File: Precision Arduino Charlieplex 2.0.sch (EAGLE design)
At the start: 265 parts, among them J402 EM406, J404 EM406, U401 ATMEGA328, U501 FT232RLSSOP, U602 ZF7, Y401 12.00

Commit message: Merged Mio's KwanSystems.lbr, updated all eagle files to use it.
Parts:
- removed D200, D201, D202, D203, D204, D205, D206, D207, D208, D209, D210, D211, D212, D213, D214, D215, D216, D217, D218, D219, D220, D221, D222, D223, D224, D225, D226, D227, D228, D229, D230, D231, D232, D233, D234, D235, D236, D237, D238, D239, D240, D241, D242, D243, D244, D245, D246, D247, D248, D249, D250, D251, D252, D253, D254, D255, D256, D257, D258, D259, D300, D301, D302, D303, D304, D305, D306, D307, D308, D309, D310, D311, D312, D313, D314, D315, D316, D317, D318, D319, D320, D321, D322, D323, D324, D325, D326, D327, D328, D329, D330, D331, D332, D333, D334, D335, D336, D337, D338, D339, D340, D341, D342, D343, D344, D345, D346, D347, D348, D349, D350, D351, D352, D353, D354, D355, D356, D357, D358, D359: HOUR, SparkFun:LED0603
- removed J402, J404: EM406, SparkFun:EM406
- removed SJ1: (no value), SparkFun:SOLDERJUMPER_2WAYS
- added D060, D061, D062: HOUR, SparkFun:LED0603
- added J001, J004: (no value), SparkFun:M04PTH
- added J005: (no value), SparkFun:M06SIP
- added J405, J406: (no value), SparkFun:M081X08
- added JP1, JP2, JP3, JP4: STAND-OFF, SparkFun:STAND-OFF
- added JP5: (no value), SparkFun:M02PTH
- D501: value RED -> BLUE
- D502: value BLUE -> RED
- S429: value B3U-1100P -> B3U-1000P; device KwanSystems:B3U-1100P -> KwanSystems:B3U-1000P
- Y401: value 12.00 -> 16MHz
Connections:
- new net 3V3: J004.4, JP5.1, U501.3V3OUT
- net AT_RX: no longer SJ1.2
- net AT_TX: now also J004.1; no longer J402.RX, J404.RX
- net D12: now also J005.5
- net GND: now also J001.4, J004.3, J005.3, S429.1; no longer J402.GND1, J402.GND2, J404.GND1, J404.GND2, S429G.1, S429S.1, Y401G$1.1
- net GPS_TX: now also J004.2; no longer J402.TX, J404.TX, SJ1.1
- net P01: now also J005.6
- net P16: now also J005.4
- net PPS: now also JP5.2; no longer J402.1PPS, J404.1PPS
- net Q01: now also D060.A, D061.A, J406.1; no longer D200.A, D215.A, D229.A, D242.A, D254.A, D305.A, D315.A, D324.A, D332.A, D339.A, D345.A, D350.A, D354.A, D357.A, D359.A
- net Q02: now also D062.A, J406.2; no longer D200.C, D201.A, D216.A, D230.A, D243.A, D255.A, D306.A, D316.A, D325.A, D333.A, D340.A, D346.A, D351.A, D355.A, D358.A
- net Q03: now also J406.3; no longer D201.C, D202.A, D215.C, D217.A, D231.A, D244.A, D256.A, D307.A, D317.A, D326.A, D334.A, D341.A, D347.A, D352.A, D356.A
- net Q04: now also J406.4; no longer D202.C, D203.A, D216.C, D218.A, D229.C, D232.A, D245.A, D257.A, D308.A, D318.A, D327.A, D335.A, D342.A, D348.A, D353.A
- net Q05: now also J406.5; no longer D203.C, D204.A, D217.C, D219.A, D230.C, D233.A, D242.C, D246.A, D258.A, D309.A, D319.A, D328.A, D336.A, D343.A, D349.A
- net Q06: now also J406.6; no longer D204.C, D205.A, D218.C, D220.A, D231.C, D234.A, D243.C, D247.A, D254.C, D259.A, D310.A, D320.A, D329.A, D337.A, D344.A
- net Q07: now also J406.7; no longer D205.C, D206.A, D219.C, D221.A, D232.C, D235.A, D244.C, D248.A, D255.C, D300.A, D305.C, D311.A, D321.A, D330.A, D338.A
- net Q08: now also J406.8; no longer D206.C, D207.A, D220.C, D222.A, D233.C, D236.A, D245.C, D249.A, D256.C, D301.A, D306.C, D312.A, D315.C, D322.A, D331.A
- net Q09: now also J405.1; no longer D207.C, D208.A, D221.C, D223.A, D234.C, D237.A, D246.C, D250.A, D257.C, D302.A, D307.C, D313.A, D316.C, D323.A, D324.C
- net Q10: now also J405.2; no longer D208.C, D209.A, D222.C, D224.A, D235.C, D238.A, D247.C, D251.A, D258.C, D303.A, D308.C, D314.A, D317.C, D325.C, D332.C
- net Q11: now also J405.3; no longer D209.C, D210.A, D223.C, D225.A, D236.C, D239.A, D248.C, D252.A, D259.C, D304.A, D309.C, D318.C, D326.C, D333.C, D339.C
- net Q12: now also J405.4; no longer D210.C, D211.A, D224.C, D226.A, D237.C, D240.A, D249.C, D253.A, D300.C, D310.C, D319.C, D327.C, D334.C, D340.C, D345.C
- net Q13: now also J405.5; no longer D211.C, D212.A, D225.C, D227.A, D238.C, D241.A, D250.C, D301.C, D311.C, D320.C, D328.C, D335.C, D341.C, D346.C, D350.C
- net Q14: now also J405.6; no longer D212.C, D213.A, D226.C, D228.A, D239.C, D251.C, D302.C, D312.C, D321.C, D329.C, D336.C, D342.C, D347.C, D351.C, D354.C
- net Q15: now also J405.7; no longer D213.C, D214.A, D227.C, D240.C, D252.C, D303.C, D313.C, D322.C, D330.C, D337.C, D343.C, D348.C, D352.C, D355.C, D357.C
- net Q16: now also J405.8; no longer D214.C, D228.C, D241.C, D253.C, D304.C, D314.C, D323.C, D331.C, D338.C, D344.C, D349.C, D353.C, D356.C, D358.C, D359.C
- net RESET: now also J005.1, S429.2; no longer S429S.2
- net USBD+: now also J001.1
- net USBD-: now also J001.2
- net USB_TX: no longer SJ1.3
- net VCC: now also J001.3, J005.2; no longer J402.VCC, J404.VCC
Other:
- moved on the sheet: C010, C408, D000, D001, D002, D003, D004, D005, D006, D007, D008, D009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

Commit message: Preparing for check against workspace~ and workspace2
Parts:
- removed D060, D061, D062: HOUR, SparkFun:LED0603
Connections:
- net GND: now also Y401.GND
- net Q01: no longer D060.A, D061.A
- net Q02: no longer D062.A
- net XTAL1: now also Y401.1; no longer Y401_.1
- net XTAL2: now also Y401.2; no longer Y401_.2
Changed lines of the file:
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@@
 <part name="JP5" library="SparkFun" deviceset="M02" device="PTH"/>
 <part name="GND3" library="SparkFun" deviceset="GND" device=""/>
-<part name="D060" library="SparkFun" deviceset="LED" device="0603" value="HOUR"/>
-<part name="D061" library="SparkFun" deviceset="LED" device="0603" value="HOUR"/>
-<part name="D062" library="SparkFun" deviceset="LED" device="0603" value="HOUR"/>
 </parts>
 <sheets>
@@
 <instance part="C408" gate="G$1" x="-254" y="88.9" rot="R90"/>
 <instance part="GND4" gate="1" x="-261.62" y="53.34"/>
-<instance part="Y401" gate="_" x="-246.38" y="91.44" rot="R270"/>
+<instance part="Y401" gate="G$1" x="-246.38" y="91.44" rot="R270"/>
 <instance part="J001" gate="G$1" x="-149.86" y="147.32" rot="MR180"/>
 <instance part="J002" gate="G$1" x="-137.16" y="147.32" rot="MR180"/>
@@
 <instance part="JP5" gate="G$1" x="-129.54" y="50.8" rot="R180"/>
 <instance part="GND3" gate="1" x="-154.94" y="55.88" rot="MR0"/>
-<instance part="D060" gate="G$1" x="142.24" y="25.4" smashed="yes" rot="R180">
-<attribute name="NAME" x="142.7226" y="22.86" size="1.778" layer="95" rot="R270"/>
-</instance>
-<instance part="D061" gate="G$1" x="132.08" y="25.4" smashed="yes" rot="R180">
-<attribute name="NAME" x="132.5626" y="22.86" size="1.778" layer="95" rot="R270"/>
-</instance>
-<instance part="D062" gate="G$1" x="132.08" y="38.1" smashed="yes" rot="R180">
-<attribute name="NAME" x="132.5626" y="35.56" size="1.778" layer="95" rot="R270"/>
-</instance>
 </instances>
 <busses>
@@
 <segment>
 <wire x1="-17.78" y1="22.86" x2="132.08" y2="22.86" width="0.1524" layer="91"/>
-<wire x1="132.08" y1="22.86" x2="139.7" y2="22.86" width="0.1524" layer="91"/>
 <wire x1="139.7" y1="22.86" x2="132.08" y2="22.86" width="0.1524" layer="91"/>
 <wire x1="132.08" y1="22.86" x2="129.54" y2="22.86" width="0.1524" layer="91"/>
@@
 <pinref part="D159" gate="G$1" pin="C"/>
 <pinref part="J406" gate="G$1" pin="1"/>
-<wire x1="139.7" y1="22.86" x2="142.24" y2="22.86" width="0.1524" layer="91"/>
-<wire x1="142.24" y1="22.86" x2="144.78" y2="22.86" width="0.1524" layer="91"/>
+<wire x1="139.7" y1="22.86" x2="144.78" y2="22.86" width="0.1524" layer="91"/>
 <wire x1="144.78" y1="22.86" x2="144.78" y2="-17.78" width="0.1524" layer="91"/>
 <wire x1="144.78" y1="-17.78" x2="30.48" y2="-17.78" width="0.1524" layer="91"/>
 <wire x1="30.48" y1="-17.78" x2="30.48" y2="-20.32" width="0.1524" layer="91"/>
 <label x="144.78" y="17.78" size="1.778" layer="95" rot="R90"/>
-<pinref part="D060" gate="G$1" pin="A"/>
-<junction x="142.24" y="22.86"/>
-<pinref part="D061" gate="G$1" pin="A"/>
 <junction x="132.08" y="22.86"/>
 </segment>
@@
 <pinref part="D000" gate="G$1" pin="A"/>
 <pinref part="J406" gate="G$1" pin="2"/>
-<wire x1="129.54" y1="35.56" x2="132.08" y2="35.56" width="0.1524" layer="91"/>
-<wire x1="132.08" y1="35.56" x2="134.62" y2="35.56" width="0.1524" layer="91"/>
+<wire x1="129.54" y1="35.56" x2="134.62" y2="35.56" width="0.1524" layer="91"/>
 <wire x1="134.62" y1="35.56" x2="134.62" y2="30.48" width="0.1524" layer="91"/>
 <wire x1="139.7" y1="30.48" x2="134.62" y2="30.48" width="0.1524" layer="91"/>
@@
 <label x="134.62" y="17.78" size="1.778" layer="95" rot="R90"/>
 <junction x="134.62" y="30.48"/>
-<pinref part="D062" gate="G$1" pin="A"/>
-<junction x="132.08" y="35.56"/>
 </segment>
 </net>
@@
 <wire x1="-259.08" y1="88.9" x2="-261.62" y2="88.9" width="0.1524" layer="91"/>
 <wire x1="-261.62" y1="88.9" x2="-261.62" y2="68.58" width="0.1524" layer="91"/>
-<wire x1="-261.62" y1="93.98" x2="-261.62" y2="88.9" width="0.1524" layer="91"/>
+<wire x1="-261.62" y1="93.98" x2="-261.62" y2="91.44" width="0.1524" layer="91"/>
+<wire x1="-261.62" y1="91.44" x2="-261.62" y2="88.9" width="0.1524" layer="91"/>
 <wire x1="-259.08" y1="93.98" x2="-261.62" y2="93.98" width="0.1524" layer="91"/>
 <wire x1="-261.62" y1="104.14" x2="-261.62" y2="93.98" width="0.1524" layer="91"/>
@@
 <pinref part="C420" gate="G$1" pin="2"/>
 <pinref part="S429" gate="G$1" pin="1"/>
+<pinref part="Y401" gate="G$1" pin="GND"/>
+<wire x1="-251.46" y1="91.44" x2="-261.62" y2="91.44" width="0.1524" layer="91"/>
+<junction x="-261.62" y="91.44"/>
 </segment>
 <segment>
@@
 <label x="-241.3" y="93.98" size="1.778" layer="95"/>
 <pinref part="C407" gate="G$1" pin="2"/>
-<pinref part="Y401" gate="_" pin="1"/>
+<pinref part="Y401" gate="G$1" pin="1"/>
 <pinref part="U401" gate="G$1" pin="PB6(XTAL1/TOSC1)"/>
 </segment>
@@
 <label x="-241.3" y="78.74" size="1.778" layer="95"/>
 <pinref part="C408" gate="G$1" pin="2"/>
-<pinref part="Y401" gate="_" pin="2"/>
+<pinref part="Y401" gate="G$1" pin="2"/>
 <pinref part="U401" gate="G$1" pin="PB7(XTAL2/TOSC2)"/>
 </segment>

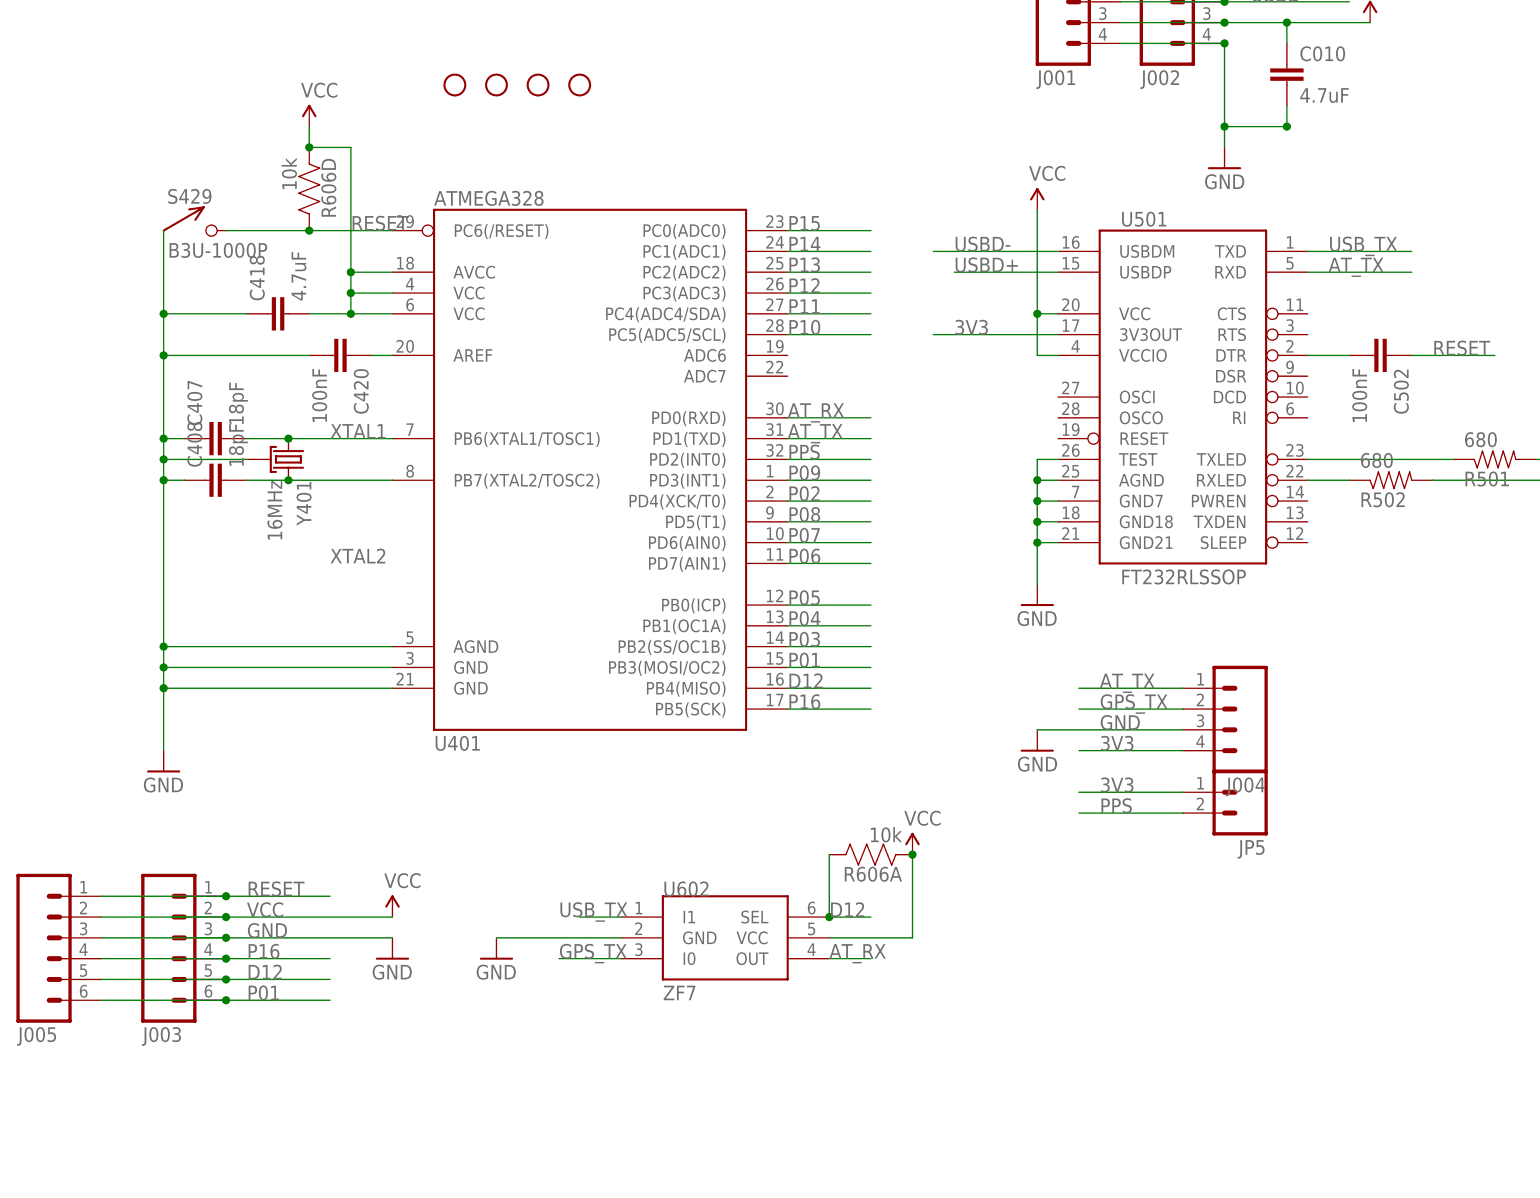
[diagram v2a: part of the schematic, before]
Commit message: Started RocketometerATMega.sch, finished PrecisionATMega32U4
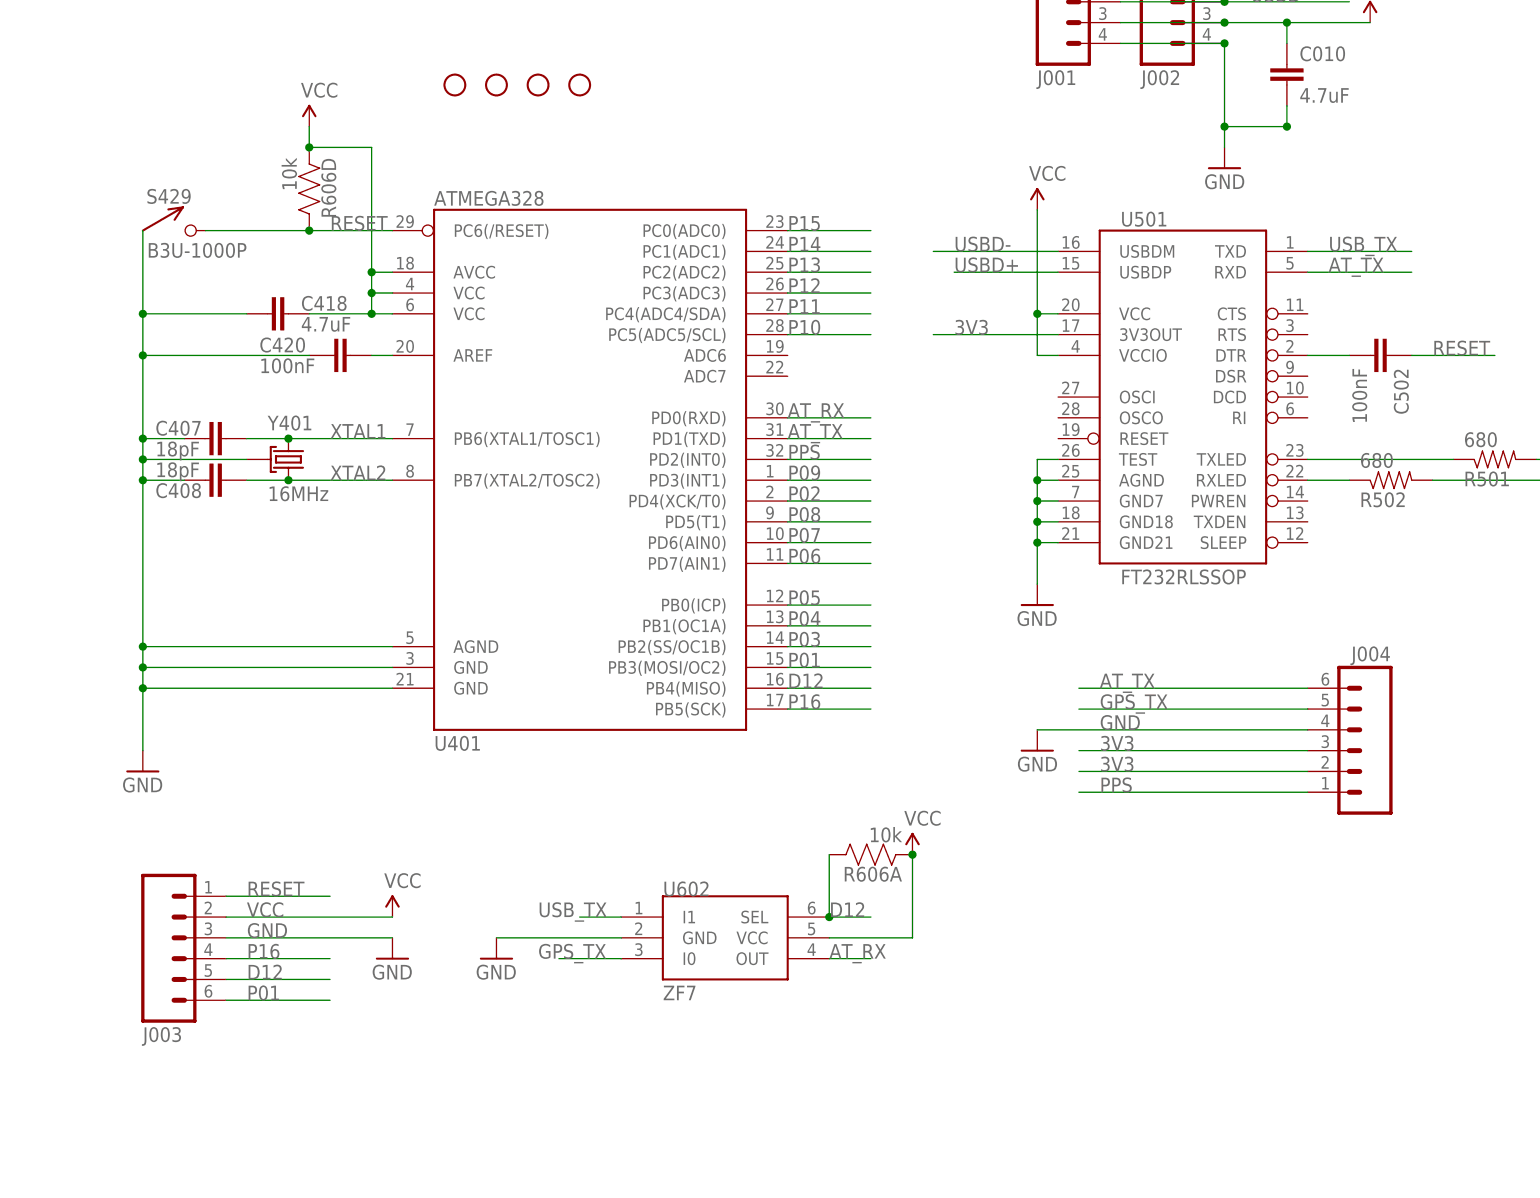
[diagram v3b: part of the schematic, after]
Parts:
- removed J005: (no value), SparkFun:M06SIP
- removed JP5: (no value), SparkFun:M02PTH
- J004: device SparkFun:M04PTH -> SparkFun:M06SIP
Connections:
- net 3V3: now also J004.2, J004.3; no longer J004.4, JP5.1
- net AT_TX: now also J004.6; no longer J004.1
- net D12: no longer J005.5
- net GND: now also J004.4; no longer J004.3, J005.3
- net GPS_TX: now also J004.5; no longer J004.2
- net P01: no longer J005.6
- net P16: no longer J005.4
- net PPS: now also J004.1; no longer JP5.2
- net RESET: no longer J005.1
- net VCC: no longer J005.2
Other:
- moved on the sheet: S429
